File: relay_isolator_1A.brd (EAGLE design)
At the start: 44 x 44 mm, 10 parts

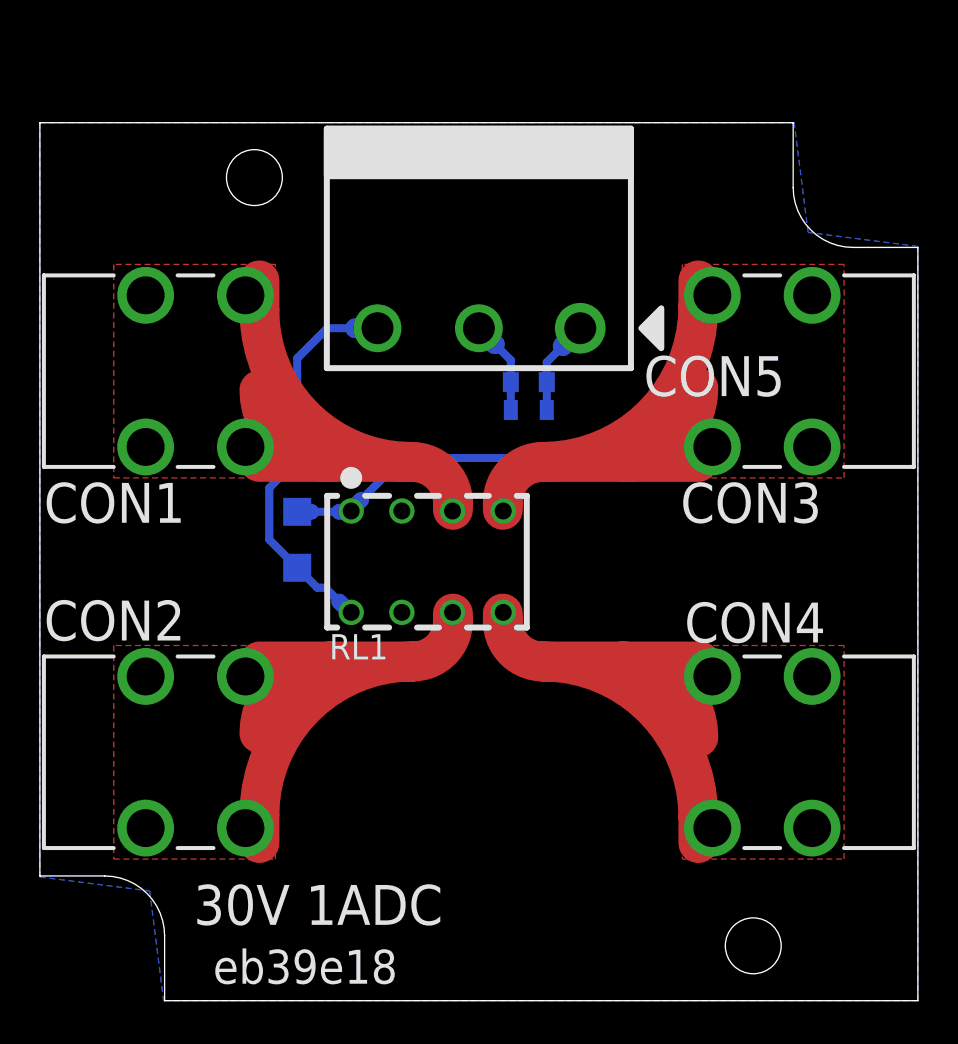
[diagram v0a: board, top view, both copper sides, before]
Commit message: update layout and library
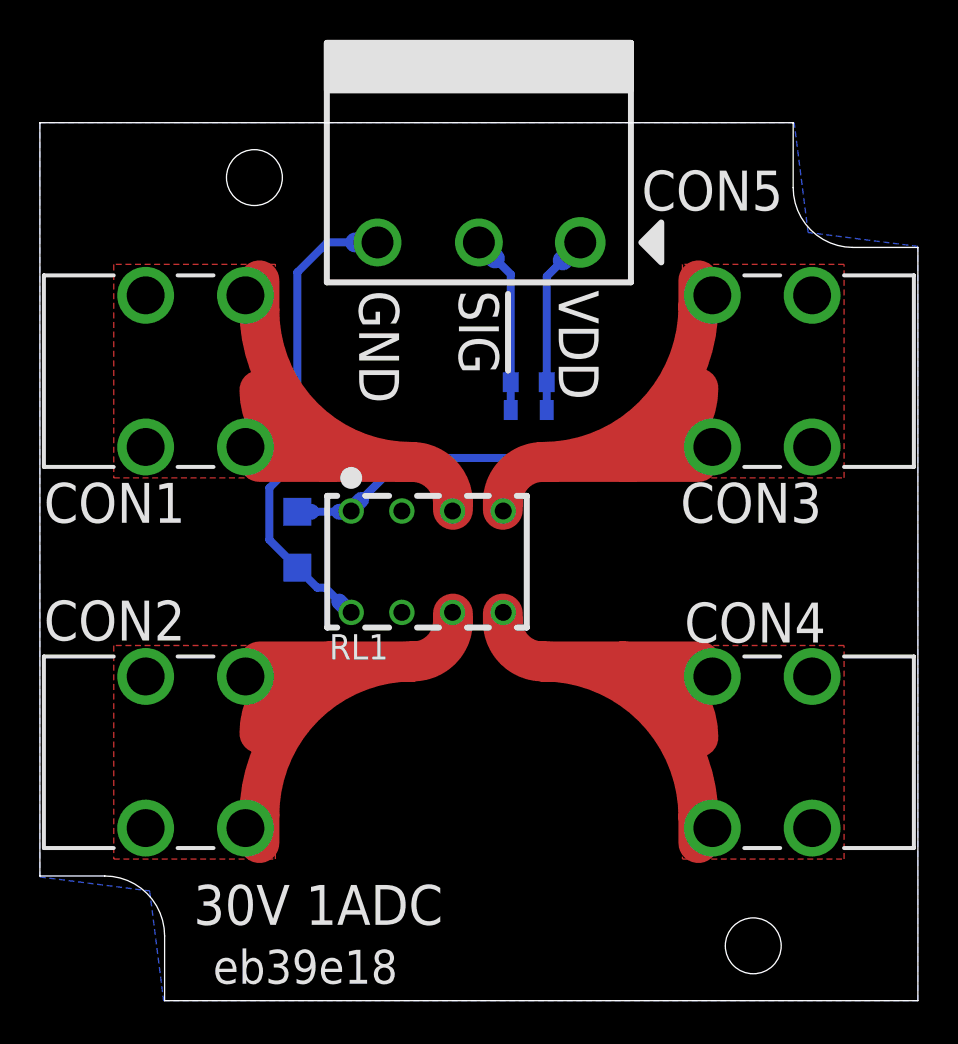
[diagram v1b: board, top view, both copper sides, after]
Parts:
- moved CON5 4.30 mm to (22.0, 38.0)
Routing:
- net VDD: track 4.82 -> 9.12 mm
- net GND: track 20.1 -> 24.4 mm
- net !SIG!: track 4.76 -> 9.06 mm
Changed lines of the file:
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@@
 <layer number="49" name="Reference" color="7" fill="1" visible="no" active="yes"/>
 <layer number="50" name="dxf" color="7" fill="1" visible="no" active="yes"/>
-<layer number="51" name="tDocu" color="7" fill="1" visible="no" active="yes"/>
+<layer number="51" name="tDocu" color="7" fill="1" visible="yes" active="yes"/>
 <layer number="52" name="bDocu" color="7" fill="1" visible="no" active="yes"/>
 <layer number="53" name="tGND_GNDA" color="7" fill="9" visible="no" active="no"/>
@@
 <plain>
 <text x="7.7" y="3.8" size="2" layer="21" ratio="15">30V 1ADC</text>
-<text x="26.1" y="35.5" size="2" layer="22" ratio="15" rot="SMR90">VDD</text>
-<text x="21.1" y="35.5" size="2" layer="22" ratio="15" rot="SMR90">!SIG!</text>
-<text x="16.1" y="35.5" size="2" layer="22" ratio="15" rot="SMR90">GND</text>
+<text x="26" y="35.6" size="2" layer="21" ratio="15" rot="SR270">VDD</text>
+<text x="21" y="35.6" size="2" layer="21" ratio="15" rot="SR270">!SIG!</text>
+<text x="16" y="35.6" size="2" layer="21" ratio="15" rot="SR270">GND</text>
 <wire x1="6.25" y1="0" x2="44" y2="0" width="0" layer="20"/>
 <wire x1="44" y1="0" x2="44" y2="37.75" width="0" layer="20"/>
@@
 <attribute name="VALUE" x="24.5" y="28.4" size="1" layer="28" font="vector" rot="MR180" align="center"/>
 </element>
-<element name="CON5" library="mylib" package="ETB43034" value="" x="22" y="33.7" smashed="yes" rot="SR180">
-<attribute name="NAME" x="33.8" y="31.3" size="2" layer="25" ratio="15" rot="SR0" align="center"/>
-<attribute name="AKIZUKI" value="P-11590" x="22" y="33.7" size="1.778" layer="27" rot="SR180" display="off"/>
+<element name="CON5" library="mylib" package="ETB43034" value="" x="22" y="38" smashed="yes" rot="SR180">
+<attribute name="NAME" x="33.7" y="40.6" size="2" layer="25" ratio="15" rot="SR0" align="center"/>
+<attribute name="AKIZUKI" value="P-11590" x="22" y="38" size="1.778" layer="27" rot="SR180" display="off"/>
 </element>
 <element name="R1" library="mylib" package="R-1608-PADPAD" value="" x="24.5" y="31" smashed="yes" rot="MR180">
@@
 <contactref element="D1" pad="A"/>
 <contactref element="CON5" pad="3"/>
-<wire x1="12.9" y1="32.2" x2="12.9" y2="27.1" width="0.4" layer="16"/>
+<wire x1="12.9" y1="36.5" x2="12.9" y2="27.1" width="0.4" layer="16"/>
 <wire x1="12.9" y1="27.1" x2="11.5" y2="25.7" width="0.4" layer="16"/>
 <wire x1="11.5" y1="25.7" x2="11.5" y2="23.1" width="0.4" layer="16"/>
 <wire x1="11.5" y1="23.1" x2="12.9" y2="21.7" width="0.4" layer="16"/>
-<wire x1="16.92" y1="33.7" x2="16.92" y2="33.62" width="0.4" layer="16"/>
-<wire x1="16.92" y1="33.62" x2="16.9" y2="33.6" width="0.4" layer="16"/>
-<wire x1="16.9" y1="33.6" x2="16.7" y2="33.6" width="0.4" layer="16"/>
-<wire x1="16.7" y1="33.6" x2="16.7" y2="33.7" width="0.4" layer="16"/>
-<wire x1="16.7" y1="33.7" x2="15.8" y2="33.7" width="1" layer="16"/>
-<wire x1="15.8" y1="33.7" x2="14.4" y2="33.7" width="0.4" layer="16"/>
-<wire x1="14.4" y1="33.7" x2="12.9" y2="32.2" width="0.4" layer="16"/>
+<wire x1="16.92" y1="38" x2="16.92" y2="37.92" width="0.4" layer="16"/>
+<wire x1="16.92" y1="37.92" x2="16.9" y2="37.9" width="0.4" layer="16"/>
+<wire x1="16.9" y1="37.9" x2="16.7" y2="37.9" width="0.4" layer="16"/>
+<wire x1="16.7" y1="37.9" x2="16.7" y2="38" width="0.4" layer="16"/>
+<wire x1="16.7" y1="38" x2="15.8" y2="38" width="1" layer="16"/>
+<wire x1="15.8" y1="38" x2="14.4" y2="38" width="0.4" layer="16"/>
+<wire x1="14.4" y1="38" x2="12.9" y2="36.5" width="0.4" layer="16"/>
 <wire x1="12.9" y1="21.7" x2="13.9" y2="20.7" width="0.4" layer="16"/>
 <wire x1="15.6" y1="19.46" x2="15.6" y2="19.5" width="0.4" layer="16"/>
@@
 <contactref element="R1" pad="1"/>
 <wire x1="23.6" y1="29.6" x2="23.6" y2="31" width="0.4" layer="16"/>
-<wire x1="23.6" y1="31" x2="23.6" y2="32.1" width="0.4" layer="16"/>
-<wire x1="23.6" y1="32.1" x2="22.8" y2="32.9" width="0.4" layer="16"/>
-<wire x1="22.8" y1="32.9" x2="22" y2="33.7" width="1" layer="16"/>
+<wire x1="23.6" y1="31" x2="23.6" y2="36.4" width="0.4" layer="16"/>
+<wire x1="23.6" y1="36.4" x2="22.8" y2="37.2" width="0.4" layer="16"/>
+<wire x1="22.8" y1="37.2" x2="22" y2="38" width="1" layer="16"/>
 </signal>
 <signal name="VDD">
@@
 <contactref element="R1" pad="2"/>
 <wire x1="25.4" y1="29.6" x2="25.4" y2="31" width="0.4" layer="16"/>
-<wire x1="25.4" y1="31" x2="25.4" y2="32" width="0.4" layer="16"/>
-<wire x1="25.4" y1="32" x2="26.2" y2="32.8" width="0.4" layer="16"/>
-<wire x1="26.2" y1="32.8" x2="27.1" y2="33.7" width="1" layer="16"/>
-<wire x1="27.08" y1="33.7" x2="27.1" y2="33.7" width="0.4" layer="16"/>
+<wire x1="25.4" y1="31" x2="25.4" y2="36.3" width="0.4" layer="16"/>
+<wire x1="25.4" y1="36.3" x2="26.2" y2="37.1" width="0.4" layer="16"/>
+<wire x1="26.2" y1="37.1" x2="27.1" y2="38" width="1" layer="16"/>
+<wire x1="27.08" y1="38" x2="27.1" y2="38" width="0.4" layer="16"/>
 </signal>
 <signal name="N$1">

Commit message: add T-6530 and POMONA72918 reference modules
- update library
- apply lib update for relay
- update relay and diode traces
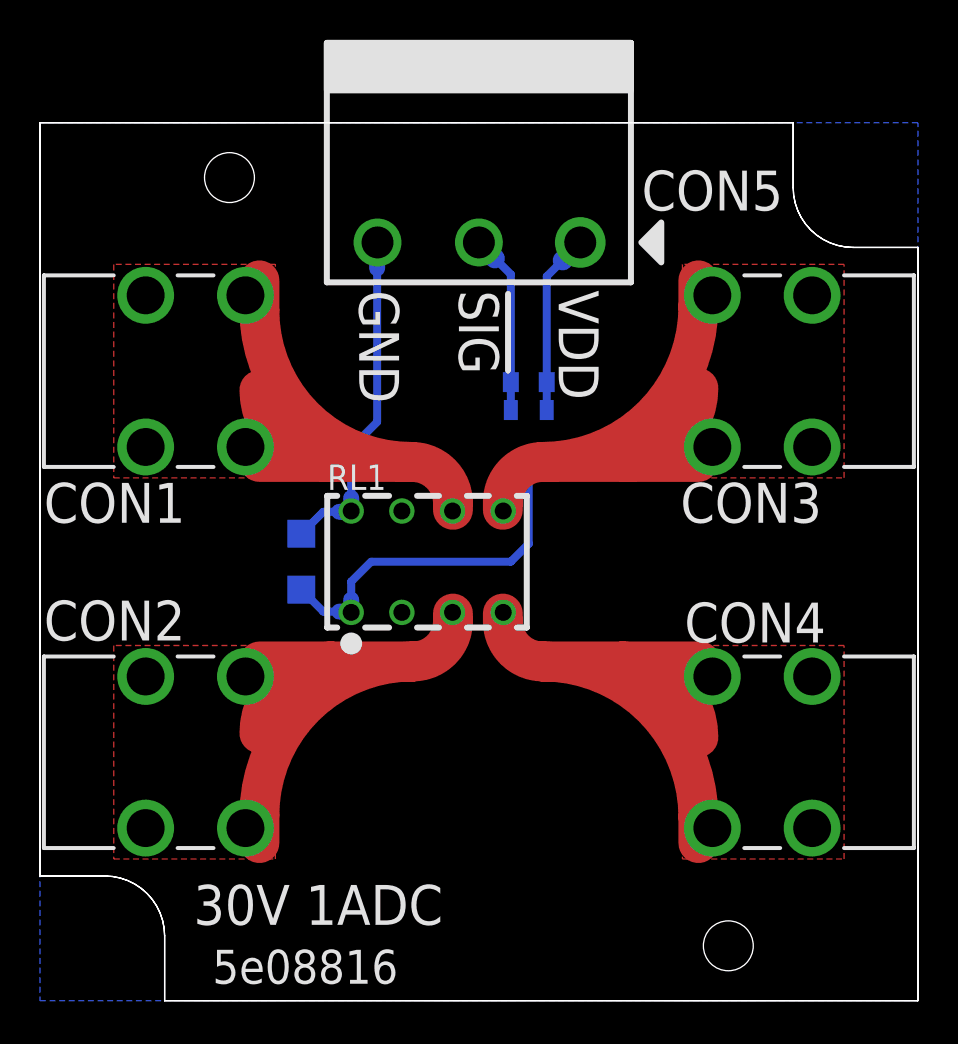
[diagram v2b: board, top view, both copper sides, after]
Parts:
- added PCB1: (no value), mylib:HAMMOND1551R
- added REF1, REF2: POMONA72918, mylib:POMONA72918
- added REF3, REF4: T-6530, mylib:T-6530
- GIT1: value eb39e18 -> 5e08816
- moved D1 1.12 mm to (13.1, 22.0), turned to 90 degrees
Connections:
- net IN-N: now also RL1.3; no longer RL1.6
- net IN-P: now also RL1.6; no longer RL1.3
- net OUT-N: now also RL1.4; no longer RL1.5
- net OUT-P: now also RL1.5; no longer RL1.4
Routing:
- net GND: track 24.4 -> 17.2 mm
- net N$5: track 12.8 -> 18.5 mm

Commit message: all components on top mount
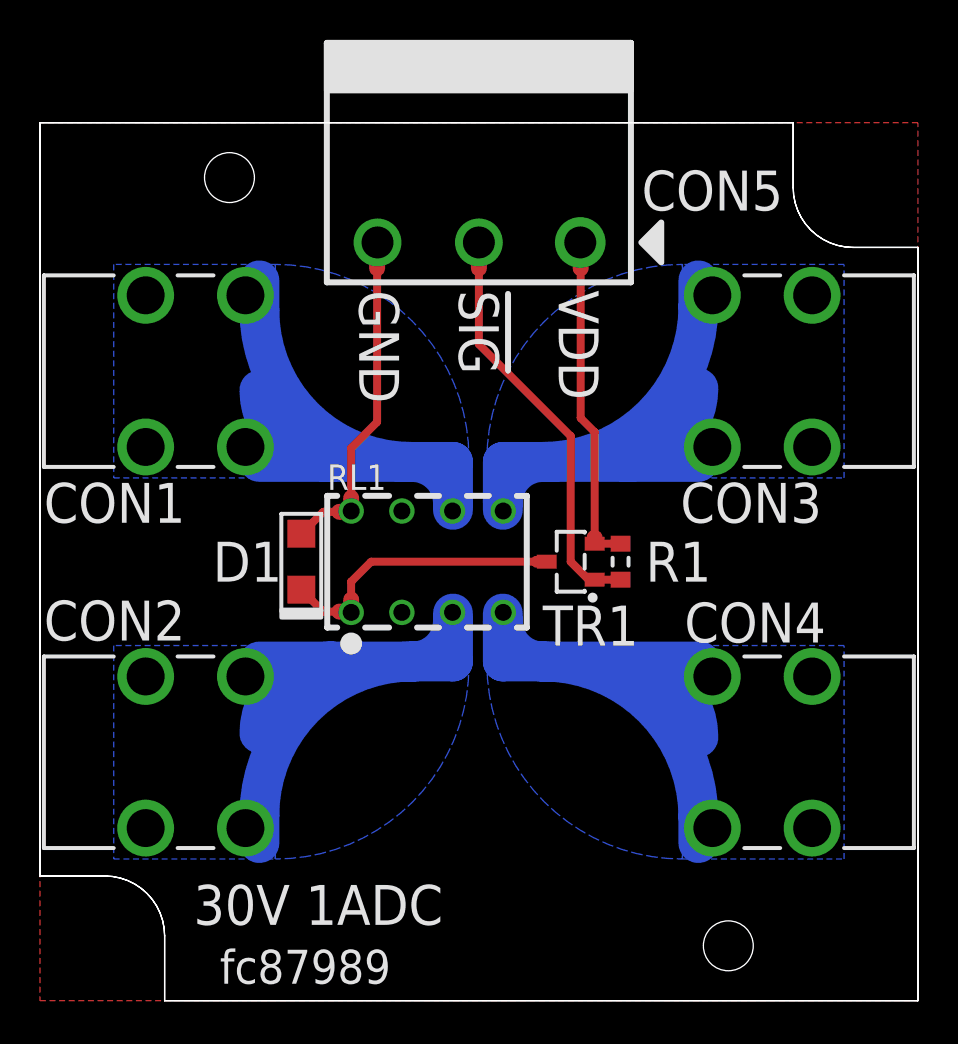
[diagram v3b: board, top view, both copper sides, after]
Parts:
- GIT1: value 5e08816 -> fc87989
- moved R1 10.1 mm to (29.1, 22.0), flipped to the top, turned to 90 degrees
- moved TR1 6.74 mm to (26.6, 22.0), flipped to the top, turned to 90 degrees
- flipped D1 to the top
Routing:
- net !SIG!: track 9.06 -> 20.8 mm
- net VDD: track 9.12 -> 16.7 mm
- net IN-P: track 28.7 -> 32.8 mm
- net OUT-P: track 29.1 -> 33.1 mm
- net IN-N: track 28.4 -> 32.4 mm
- net OUT-N: track 28.9 -> 32.9 mm
- net N$5: track 18.5 -> 14.7 mm
- added copper zone on layer 16, net IN-N
- added copper zone on layer 16, net IN-P
- added copper zone on layer 1, net N$2
- added copper zone on layer 16, net OUT-N
- added copper zone on layer 16, net OUT-P
- removed copper zone on layer 1, net IN-N
- removed copper zone on layer 1, net IN-P
- removed copper zone on layer 16, net N$2
- removed copper zone on layer 1, net OUT-N
- removed copper zone on layer 1, net OUT-P

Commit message: apply library update
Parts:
- PCB1: device mylib:HAMMOND1551R -> mylib:HAMMOND-1551R
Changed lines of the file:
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@@
 <attribute name="NOT_COMPONENT" value="YES" x="13.3" y="1.7" size="2" layer="27" ratio="20" display="off"/>
 </element>
-<element name="PCB1" library="mylib" package="HAMMOND1551R" value="" x="0" y="0">
+<element name="PCB1" library="mylib" package="HAMMOND-1551R" value="" x="0" y="0">
 <attribute name="DIGIKEY" value="HM913-ND" x="0" y="0" size="1.778" layer="27" display="off"/>
 </element>
